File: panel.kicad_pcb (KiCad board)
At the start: 2 copper layers, 92 x 100 mm, 457 parts, among them J101 Conn_01x01, J102 Conn_01x01, J103 Conn_01x01, J104 Conn_01x01, Q101 SISS27ADN-T1-GE3, Q102 Q_NMOS_GSD, U101 DRV5032FB, U102 AP7383-33WR-7, U103 ATtiny4-TS

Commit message: add a panel
Signed-off-by: Thomas Schmid <tom@binary-kitchen.de>
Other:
- board text added: "JLCJLCJLC"
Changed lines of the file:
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@@
   (general
     (thickness 1)
-    (drawings 469)
+    (drawings 470)
     (tracks 2400)
     (zones 0)
@@
       (layerselection 0x010fc_ffffffff)
       (usegerberextensions false)
-      (usegerberattributes true)
-      (usegerberadvancedattributes true)
-      (creategerberjobfile true)
+      (usegerberattributes false)
+      (usegerberadvancedattributes false)
+      (creategerberjobfile false)
       (excludeedgelayer true)
       (linewidth 0.100000)
@@
       (psa4output false)
       (plotreference true)
-      (plotvalue true)
+      (plotvalue false)
       (plotinvisibletext false)
       (padsonsilk false)
-      (subtractmaskfromsilk false)
+      (subtractmaskfromsilk true)
       (outputformat 1)
       (mirror false)
@@
     )
   )
+  (gr_text JLCJLCJLC (at 181.6 152.3) (layer F.SilkS)
+    (effects (font (size 1 1) (thickness 0.15)))
+  )
   (gr_line (start 217.6 69.3) (end 217.6 79.4) (layer Edge.Cuts) (width 0.05))

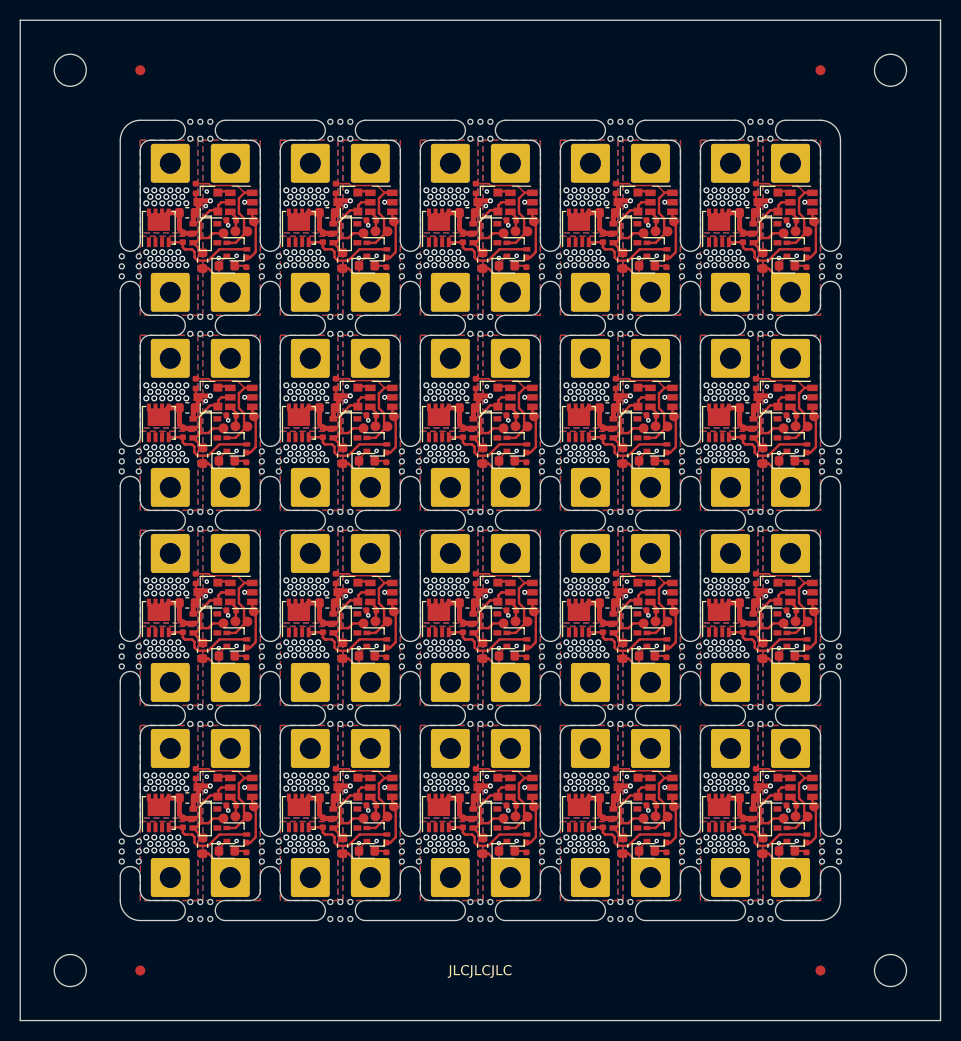
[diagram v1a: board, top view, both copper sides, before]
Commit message: fix wrongly connected power mosfet
Signed-off-by: Thomas Schmid <tom@binary-kitchen.de>
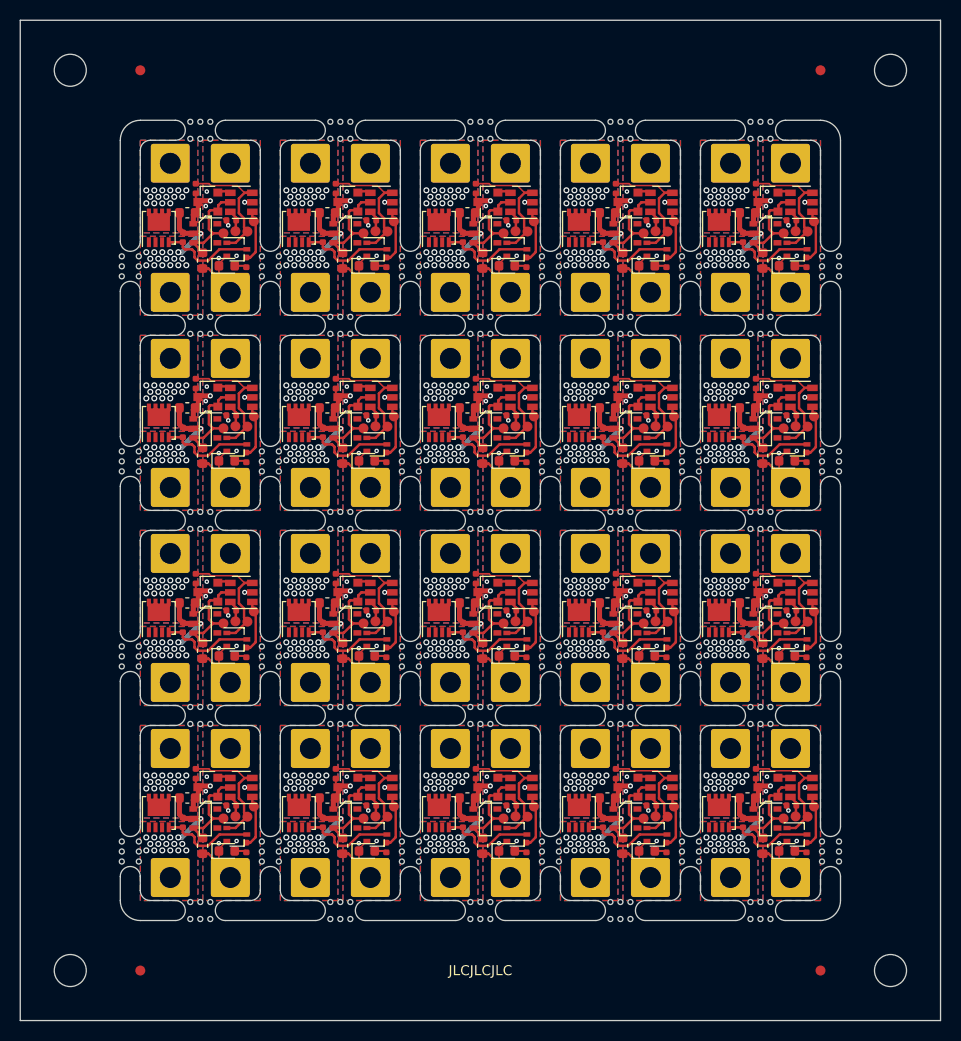
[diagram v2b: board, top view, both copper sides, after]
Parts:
- removed the REF** at (209.6, 127.8)
- removed the REF** at (195.6, 127.8)
- removed the REF** at (181.6, 127.8)
- removed the REF** at (167.6, 127.8)
- removed the REF** at (153.6, 127.8)
- removed the REF** at (209.6, 108.3)
- removed the REF** at (195.6, 108.3)
- removed the REF** at (181.6, 108.3)
- removed the REF** at (167.6, 108.3)
- removed the REF** at (153.6, 108.3)
- removed the REF** at (209.6, 88.8)
- removed the REF** at (195.6, 88.8)
- removed the REF** at (181.6, 88.8)
- removed the REF** at (167.6, 88.8)
- removed the REF** at (153.6, 88.8)
- removed the REF** at (201.6, 140.4)
- removed the REF** at (187.6, 140.4)
- removed the REF** at (173.6, 140.4)
- removed the REF** at (159.6, 140.4)
- removed the REF** at (201.6, 120.9)
- removed the REF** at (187.6, 120.9)
- removed the REF** at (173.6, 120.9)
- removed the REF** at (159.6, 120.9)
- removed the REF** at (201.6, 101.4)
- removed the REF** at (187.6, 101.4)
- removed the REF** at (173.6, 101.4)
- removed the REF** at (159.6, 101.4)
- removed the REF** at (201.6, 81.9)
- removed the REF** at (187.6, 81.9)
- removed the REF** at (173.6, 81.9)
- removed the REF** at (159.6, 81.9)
- added REF**: mousebite_3, mousebites:mousebite_double_5, F.Cu at (209.6, 125.8)
- added REF**: mousebite_3, mousebites:mousebite_double_5, F.Cu at (153.6, 106.3)
- added REF**: mousebite_3, mousebites:mousebite_double_5, F.Cu at (209.6, 86.8)
- added REF**: mousebite_3, mousebites:mousebite_double_5, F.Cu at (195.6, 86.8)
- added REF**: mousebite_3, mousebites:mousebite_double_5, F.Cu at (181.6, 86.8)
- added REF**: mousebite_3, mousebites:mousebite_double_5, F.Cu at (167.6, 86.8)
- added REF**: mousebite_3, mousebites:mousebite_double_5, F.Cu at (153.6, 86.8)
- added REF**: mousebite_3, mousebites:mousebite_double_5, F.Cu at (203.6, 140.4)
- added REF**: mousebite_3, mousebites:mousebite_double_5, F.Cu at (189.6, 140.4)
- added REF**: mousebite_3, mousebites:mousebite_double_5, F.Cu at (175.6, 140.4)
- added REF**: mousebite_3, mousebites:mousebite_double_5, F.Cu at (161.6, 140.4)
- added REF**: mousebite_3, mousebites:mousebite_double_5, F.Cu at (195.6, 125.8)
- added REF**: mousebite_3, mousebites:mousebite_double_5, F.Cu at (203.6, 120.9)
- added REF**: mousebite_3, mousebites:mousebite_double_5, F.Cu at (189.6, 120.9)
- added REF**: mousebite_3, mousebites:mousebite_double_5, F.Cu at (175.6, 120.9)
- added REF**: mousebite_3, mousebites:mousebite_double_5, F.Cu at (161.6, 120.9)
- added REF**: mousebite_3, mousebites:mousebite_double_5, F.Cu at (203.6, 101.4)
- added REF**: mousebite_3, mousebites:mousebite_double_5, F.Cu at (189.6, 101.4)
- added REF**: mousebite_3, mousebites:mousebite_double_5, F.Cu at (175.6, 101.4)
- added REF**: mousebite_3, mousebites:mousebite_double_5, F.Cu at (161.6, 101.4)
- added REF**: mousebite_3, mousebites:mousebite_double_5, F.Cu at (203.6, 81.9)
- added REF**: mousebite_3, mousebites:mousebite_double_5, F.Cu at (189.6, 81.9)
- added REF**: mousebite_3, mousebites:mousebite_double_5, F.Cu at (181.6, 125.8)
- added REF**: mousebite_3, mousebites:mousebite_double_5, F.Cu at (175.6, 81.9)
- added REF**: mousebite_3, mousebites:mousebite_double_5, F.Cu at (161.6, 81.9)
- added REF**: mousebite_3, mousebites:mousebite_double_5, F.Cu at (167.6, 125.8)
- added REF**: mousebite_3, mousebites:mousebite_double_5, F.Cu at (153.6, 125.8)
- added REF**: mousebite_3, mousebites:mousebite_double_5, F.Cu at (209.6, 106.3)
- added REF**: mousebite_3, mousebites:mousebite_double_5, F.Cu at (195.6, 106.3)
- added REF**: mousebite_3, mousebites:mousebite_double_5, F.Cu at (181.6, 106.3)
- added REF**: mousebite_3, mousebites:mousebite_double_5, F.Cu at (167.6, 106.3)
- R102 (x20): value 1k -> 10k
- turned J102 to 90 degrees (x15)
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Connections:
- J101 pad 1: VPP -> OUT (x20)
- J102 pad 1: OUT -> VPP (x20)
- Q101 pad 1: OUT -> VPP (x20)
- Q101 pad 2: OUT -> VPP (x20)
- Q101 pad 3: OUT -> VPP (x20)
- Q101 pad 5: VPP -> OUT (x20)
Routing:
- net VPP: track 112.9 -> 139.9 mm
- net +3V3: track 213.8 -> 200.9 mm
- net OUT: vias 320 -> 300
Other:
- board text added: "Alturia Magswitch V 1.1 CC BY-SA 4.0"
- board text removed: "Alturia Magswitch V 1.0 CC BY-SA 4.0"
